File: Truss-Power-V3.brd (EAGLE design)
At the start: 40.3 x 20.3 mm, 34 parts, among them J1 XF2L-0625-1, U1 TPS61090, U2 MCP73831T-2ACI/OT, U3 MAX17044, X2 MicroB, X3 22-23-2021, X4 CON-1PIN, X5 CON-1PIN

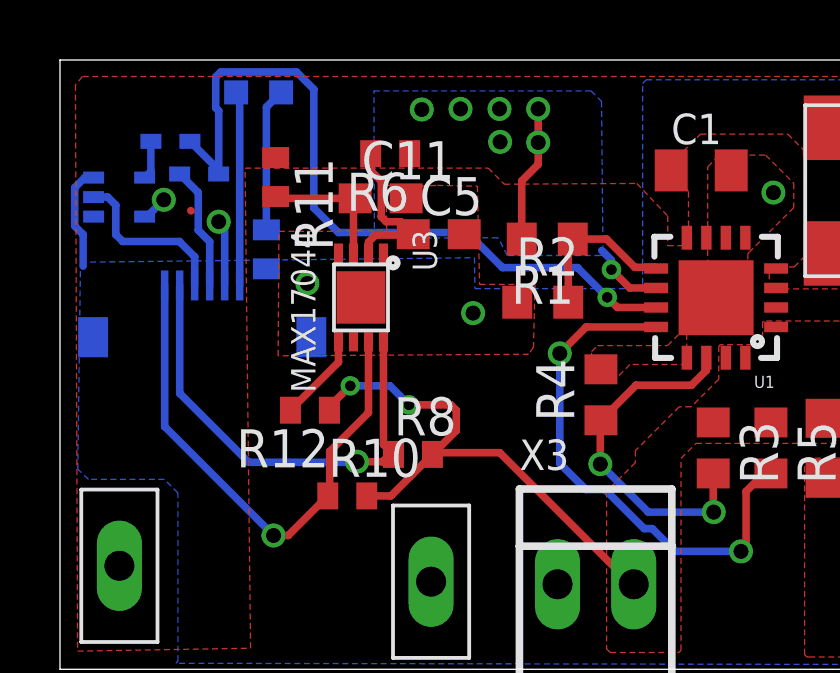
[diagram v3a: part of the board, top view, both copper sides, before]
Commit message: XOR Gate added in library; XOR gate added for Boost EN
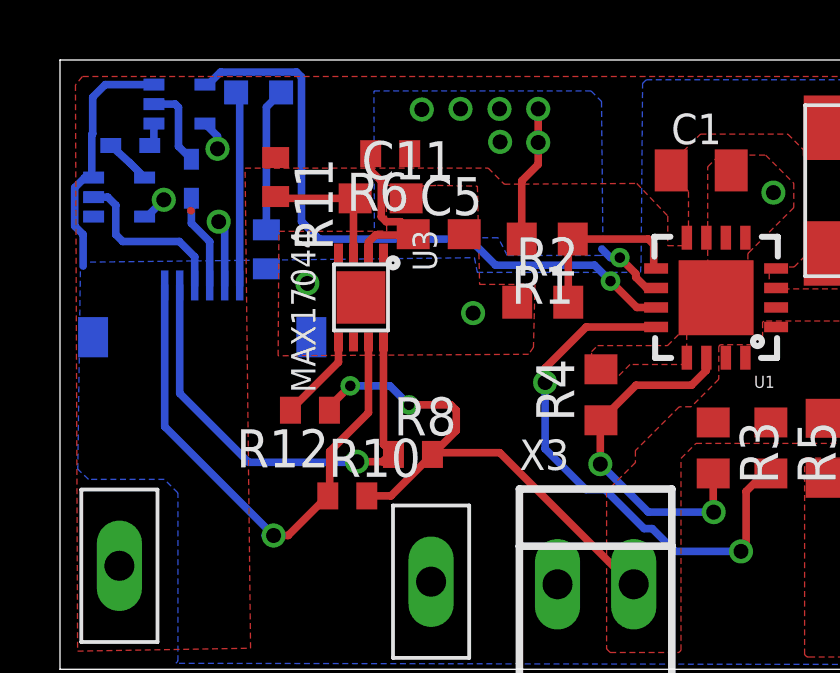
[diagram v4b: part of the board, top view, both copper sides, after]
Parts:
- added U4: SN74LVC1G86DC1LR, NewPart:SOC70-5
- moved D2 1.35 mm to (2.39, 17.5)
- moved D1 0.33 mm to (4.38, 16.4), turned to 270 degrees
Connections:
- new net DETSW_D: D2.C, U4.1
- new net PWRSW_D: D1.C, U4.2
- net EN_SIG: now also U4.4; no longer D1.C, D2.C
- net GND: now also U4.3
- net VBAT: now also U4.5
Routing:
- net GND: track 23.3 -> 28.2 mm
- net EN_SIG: track 25.1 -> 21.3 mm
- net PWRSW_D: track 0.00 -> 2.77 mm
- net PWRSW_P: track 4.13 -> 3.16 mm
- net VBAT: track 10.2 -> 11.1 mm, vias 9 -> 10
- net DETSW_D: track 0.00 -> 0.79 mm

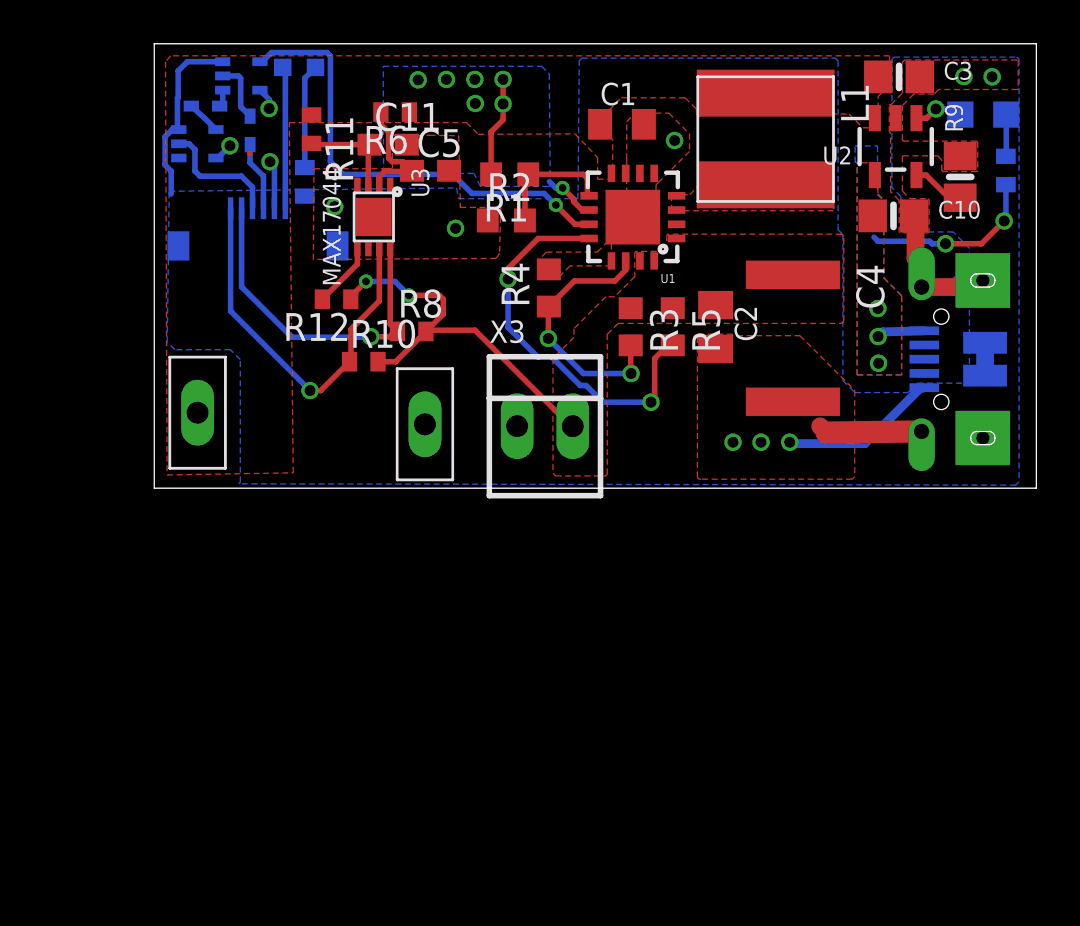
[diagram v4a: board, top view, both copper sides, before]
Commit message: To add signal control
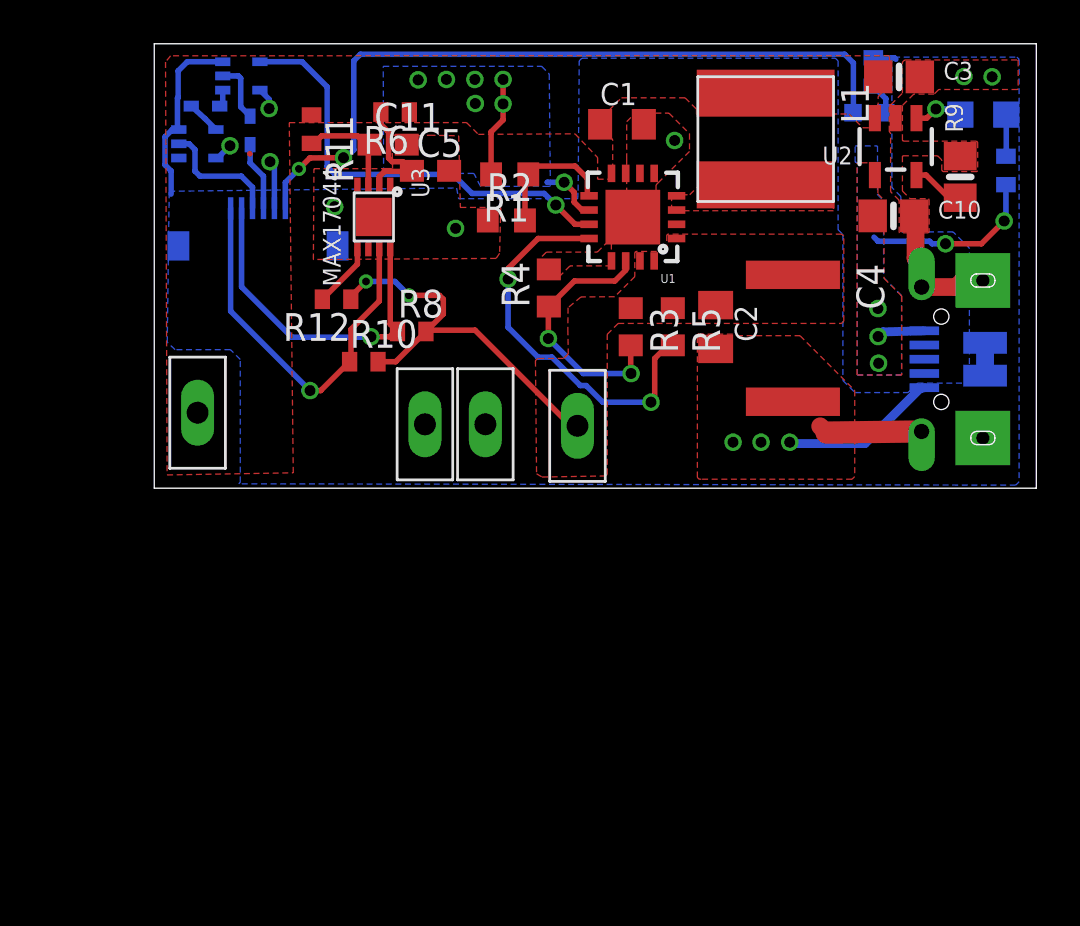
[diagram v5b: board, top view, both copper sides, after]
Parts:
- removed X3: 22-23-2021, con-molex:22-23-2021
- added X1, X6: CON-1PIN, NewPart:CON-1PIN
- moved R13 26.5 mm to (32.9, 19.0), turned to 270 degrees
- moved LED1 26.1 mm to (32.7, 17.2)
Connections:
- net GND: now also X1.P$1; no longer X3.1
- net VCC: now also X6.P$1; no longer X3.2
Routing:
- net LEDSOC: track 6.48 -> 34.4 mm, vias 0 -> 2
- net N$4: track 4.78 -> 1.45 mm
- net GND: track 28.2 -> 29.3 mm
- net EN_SIG: track 21.3 -> 20.4 mm
